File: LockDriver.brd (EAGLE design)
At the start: 25.9 x 34 mm, 19 parts, among them X1 M1, X2 M2, X3 VIN, X4 GND, X5 L, X6 U

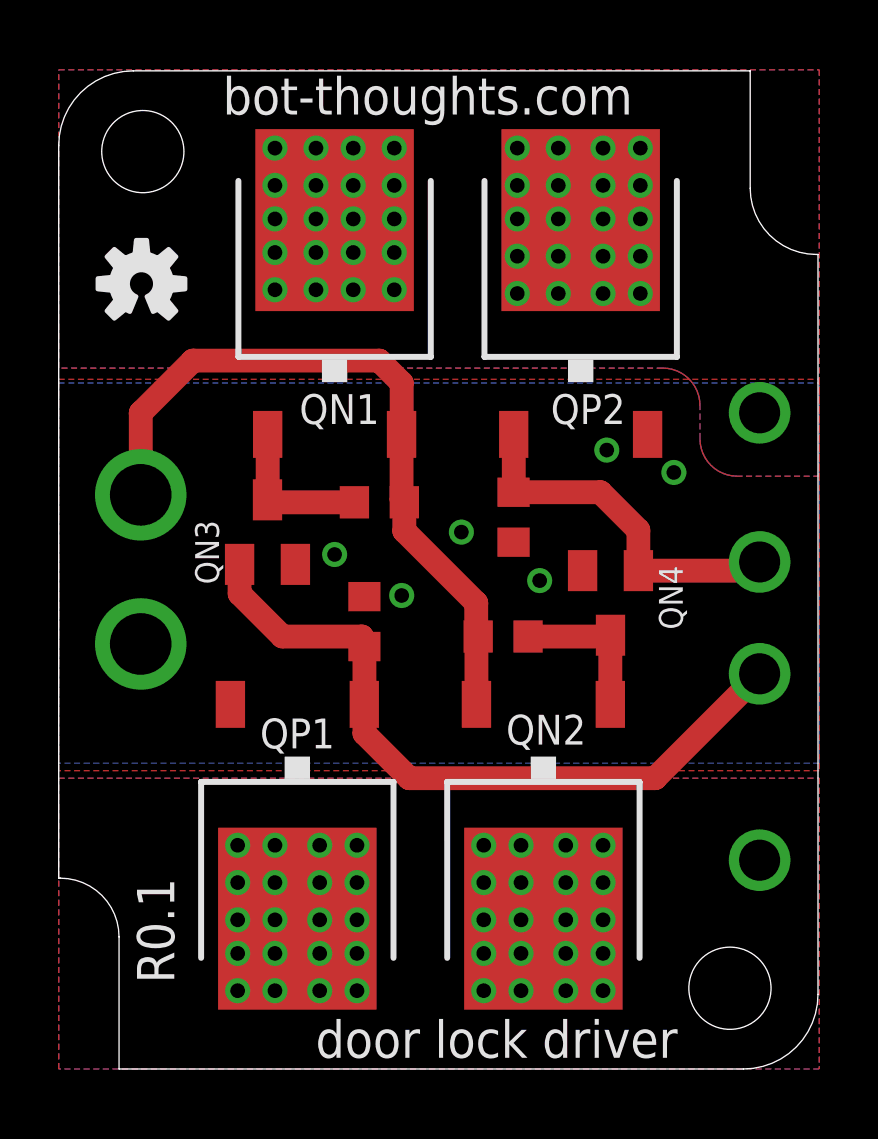
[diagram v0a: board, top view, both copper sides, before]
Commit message: added diodes, changed wirepad sizes, layout changes
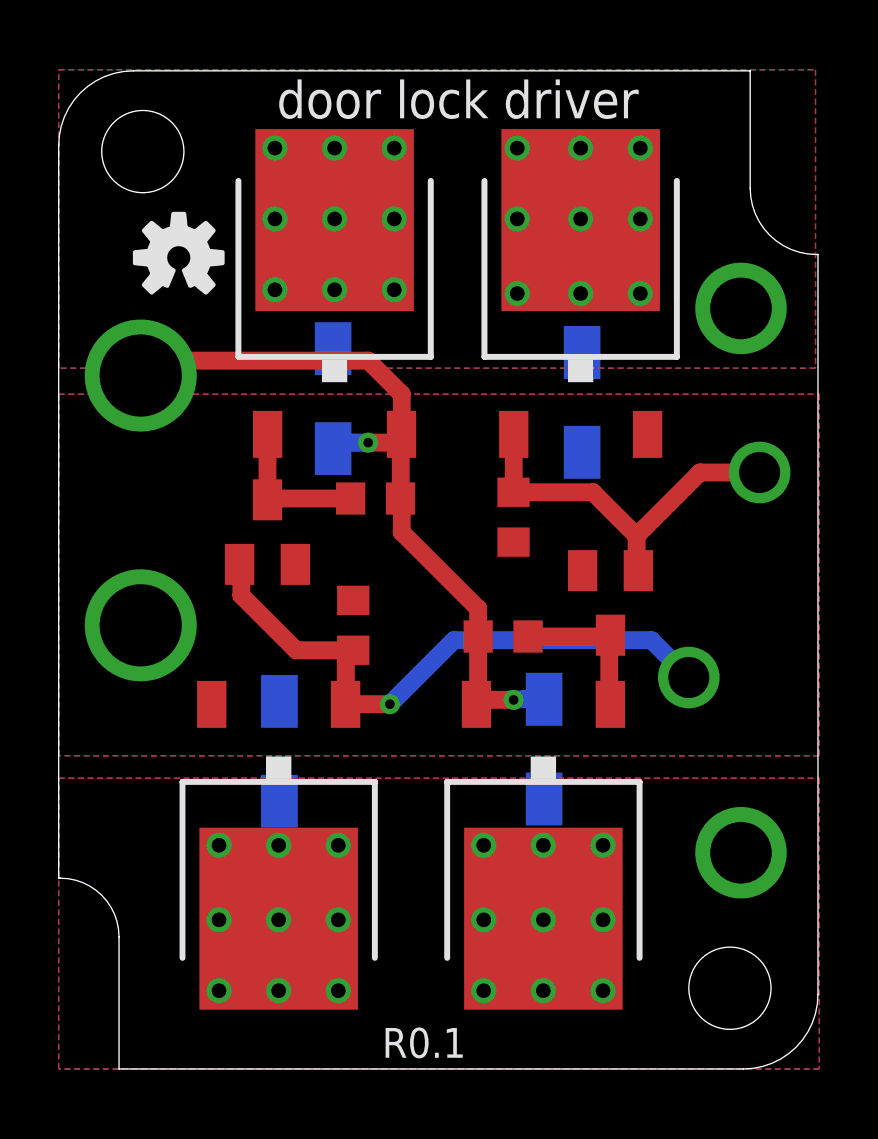
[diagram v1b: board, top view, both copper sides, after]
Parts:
- added D1, D2, D3, D4: SOD123FL, bt_diode:SOD123FL
- X1: value M1 -> S1; device bt_electromech:PAD_18GA -> bt_electromech:PAD_14GA
- X2: value M2 -> S2; device bt_electromech:PAD_18GA -> bt_electromech:PAD_14GA
- X3, X4: device bt_electromech:PAD_14GA -> bt_electromech:PAD_12GA
- X5: value L -> LOCK
- X6: value U -> UNLOCK
- moved X3 4.06 mm to (2.79, 23.6), turned to 270 degrees
- moved X1 3.61 mm to (23.2, 25.9), turned to 270 degrees
- moved X6 3.05 mm to (23.9, 20.3), turned to 270 degrees
- moved X5 2.42 mm to (21.5, 13.3)
- moved U$2 1.67 mm to (13.6, 19.4)
- moved LOGO1 1.55 mm to (4.09, 27.6)
- moved X2 0.68 mm to (23.2, 7.37), turned to 180 degrees
- moved QP1 0.63 mm to (7.49, 7.62)
- moved X4 0.63 mm to (2.79, 15.1)
- moved R3 0.40 mm to (10.0, 15.1)
- moved R1 0.18 mm to (10.8, 19.4)
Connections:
- net 12V: now also D1.C, D2.C
- net GND: now also D3.A, D4.A
- net M1: now also D1.A, D4.C
- net M2: now also D2.A, D3.C
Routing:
- net LOCK: track 24.9 -> 20.7 mm, vias 0 -> 1
- net 12V: track 24.8 -> 26.1 mm, vias 0 -> 2
- net UNLOCK: track 12.4 -> 13.1 mm
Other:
- board text added: "cc-by-sa"
